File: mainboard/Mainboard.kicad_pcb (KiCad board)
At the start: 4 copper layers, 106 x 80 mm, 142 parts, among them IC1001 TXB0104RUT, IC1002 PCA9306JK, IC1003 TXB0104RUT, IC1101 PCAL6416AHF, IC1102 TMP117xxYBG, IC1103 PCA9306JK, IC1104 PCA9633DP1,118, IC1105 RV-8263-C8, IC1201 TXB0102DCU, IC1202 PCA9306JK, IC701 USBLC6-2P6, IC702 BQ21040DBV, IC703 MAX17048, IC801 TPS62823DLC, IC802 LP5907MFX-2.8, IC803 LP5907MFX-1.5, IC804 LP5907MFX-3.0, IC805 LP5907MFX-2.8, IC806 LP5907MFX-1.2, M901 ESP32-S3-WROOM-1, Q1101 DMN2053UQ, Q1102 DMN2053UQ, Q701 Si2333CDS, SW701 On / Off, SW901 Reset, X1001 LEPTON, X1201 Camera, X1301 Micro SD-Card, X1401 Displayboard, X701 USB, X702 Battery, X901 Prog, Y1001 25 MHz, Y1201 25 MHz

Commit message: Bug: Issue #11
- Add missing name for net for TP701

Closes: #11

Signed-off-by: Daniel Kampert <danielkampert@kampis-elektroecke.de>
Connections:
- net Net-(IC702-OUT) renamed /Project Architecture/Battery/VBat
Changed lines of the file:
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@@
 	(net 114 "/Project Architecture/Display/~{Display-Expander-Int}")
 	(net 115 "Net-(IC701-VBUS)")
-	(net 116 "Net-(IC702-OUT)")
+	(net 116 "/Project Architecture/Battery/VBat")
 	(net 117 "Net-(IC701-I{slash}O2-Pad3)")
 	(net 118 "Net-(IC701-I{slash}O1-Pad1)")
@@
 			(size 1 1)
 			(layers "F.Cu" "F.Mask")
-			(net 116 "Net-(IC702-OUT)")
+			(net 116 "/Project Architecture/Battery/VBat")
 			(pinfunction "1")
 			(pintype "passive")
@@
 			(layers "F.Cu" "F.Mask" "F.Paste")
 			(roundrect_rratio 0.25)
-			(net 116 "Net-(IC702-OUT)")
+			(net 116 "/Project Architecture/Battery/VBat")
 			(pinfunction "OUT")
 			(pintype "power_out")
@@
 			(layers "B.Cu" "B.Mask" "B.Paste")
 			(roundrect_rratio 0.25)
-			(net 116 "Net-(IC702-OUT)")
+			(net 116 "/Project Architecture/Battery/VBat")
 			(pintype "passive")
 		)
@@
 			(layers "B.Cu" "B.Mask" "B.Paste")
 			(roundrect_rratio 0.222222)
-			(net 116 "Net-(IC702-OUT)")
+			(net 116 "/Project Architecture/Battery/VBat")
 			(pintype "passive")
 		)
@@
 			(layers "B.Cu" "B.Mask" "B.Paste")
 			(roundrect_rratio 0.2)
-			(net 116 "Net-(IC702-OUT)")
+			(net 116 "/Project Architecture/Battery/VBat")
 			(pintype "passive")
 		)
@@
 			(layers "B.Cu" "B.Mask" "B.Paste")
 			(roundrect_rratio 0.222222)
-			(net 116 "Net-(IC702-OUT)")
+			(net 116 "/Project Architecture/Battery/VBat")
 			(pintype "passive")
 		)

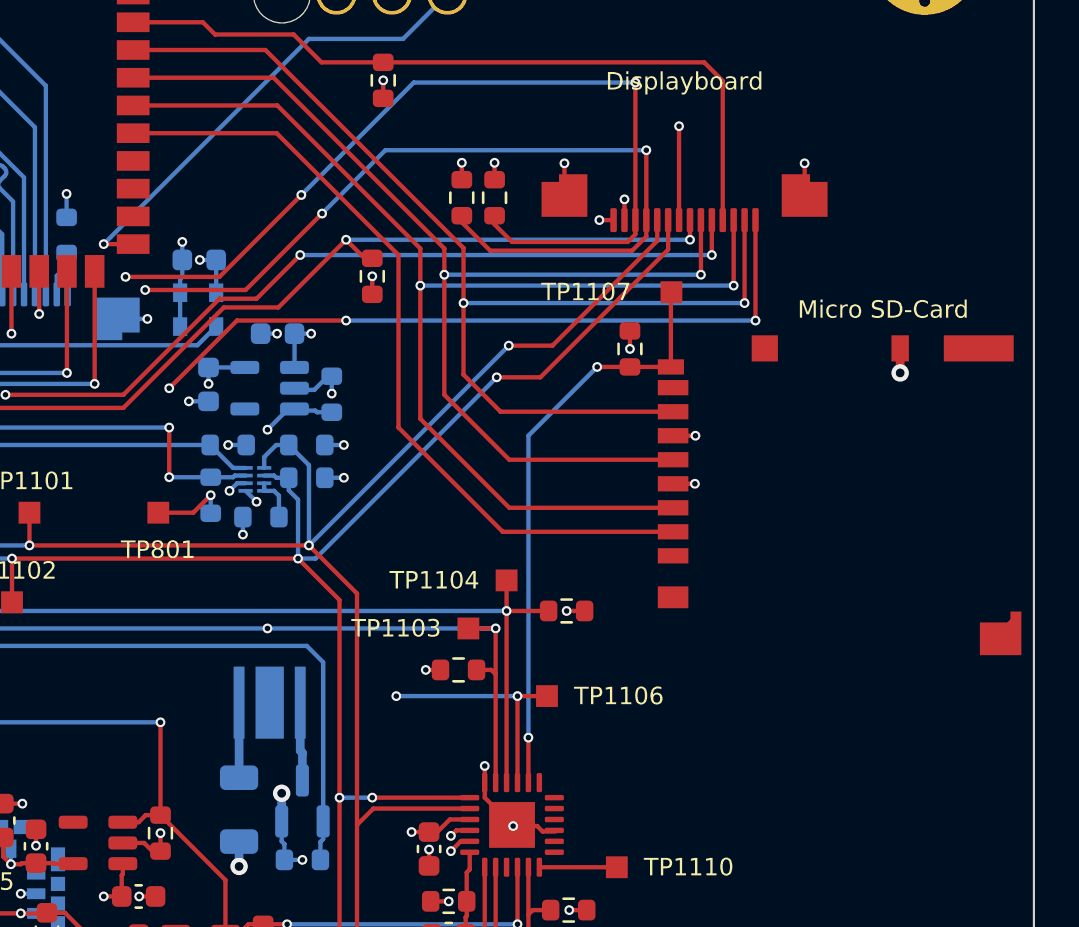
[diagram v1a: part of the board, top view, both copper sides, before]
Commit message: Feature: Issue #10
- Replace SD card holder with MSD-4-A

Closes: #10

Signed-off-by: Daniel Kampert <DanielKampert@kampis-elektroecke.de>
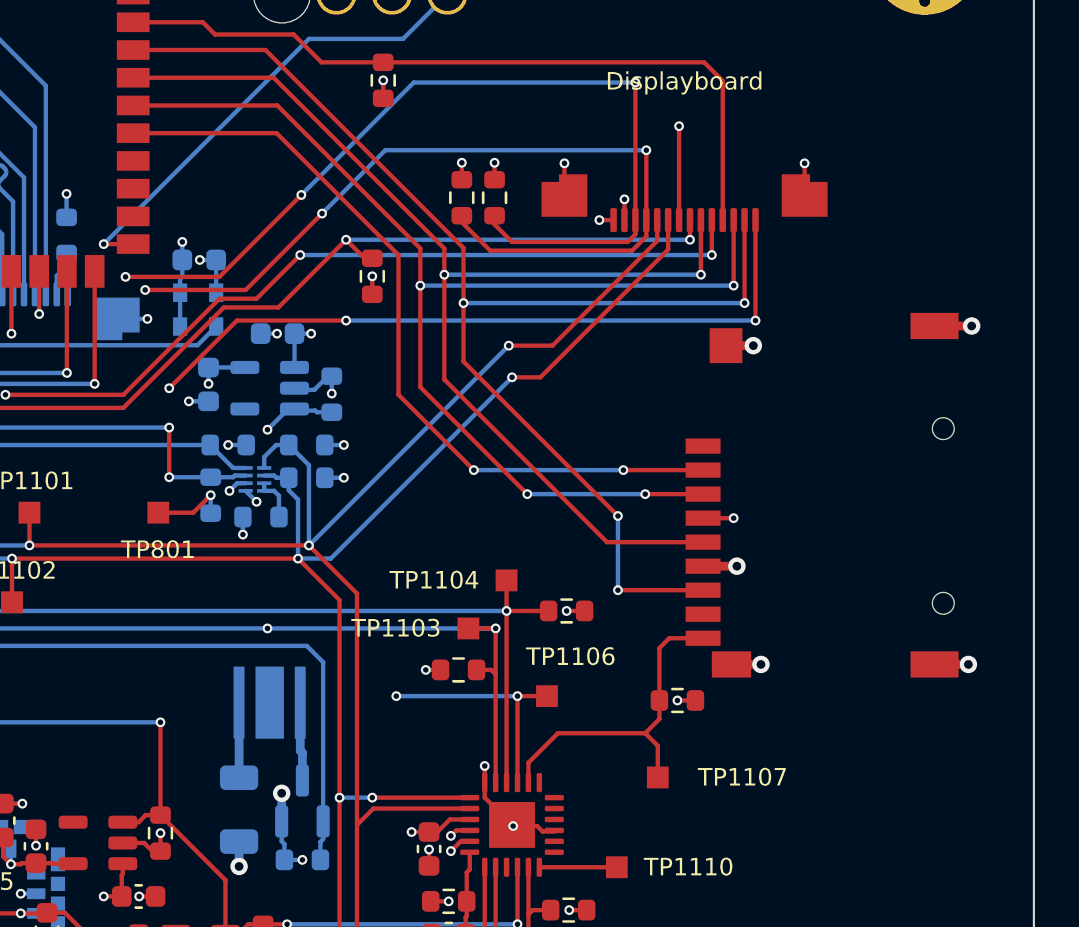
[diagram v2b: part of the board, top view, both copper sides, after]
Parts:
- X1301: footprint Connector_Card:microSD_HC_Hirose_DM3BT-DSF-PEJS -> Same Sky:MSD-4-A
- moved TP1107 22.2 mm to (248.8, 160.4), turned to 180 degrees
- moved R1301 16.2 mm to (249.7, 156.9), turned to 0 degrees
- moved X1301 1.50 mm to (258.6, 147.5)
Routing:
- net /Project Architecture/Peripherals/~{SD-CD}: track 27.2 -> 15.5 mm, vias 2 -> 0
- net /Project Architecture/Display/SPI-MISO: track 51.7 -> 58.1 mm, vias 2 -> 4
- net GND: track 123.0 -> 128.2 mm, vias 81 -> 84
- net /Project Architecture/Display/SPI-SCLK: track 50.1 -> 52.7 mm
- net /Project Architecture/MCU/~{SD-CS}: track 36.9 -> 36.2 mm, vias 0 -> 2
- net /Project Architecture/Display/SPI-MOSI: track 54.3 -> 54.5 mm, vias 2 -> 4

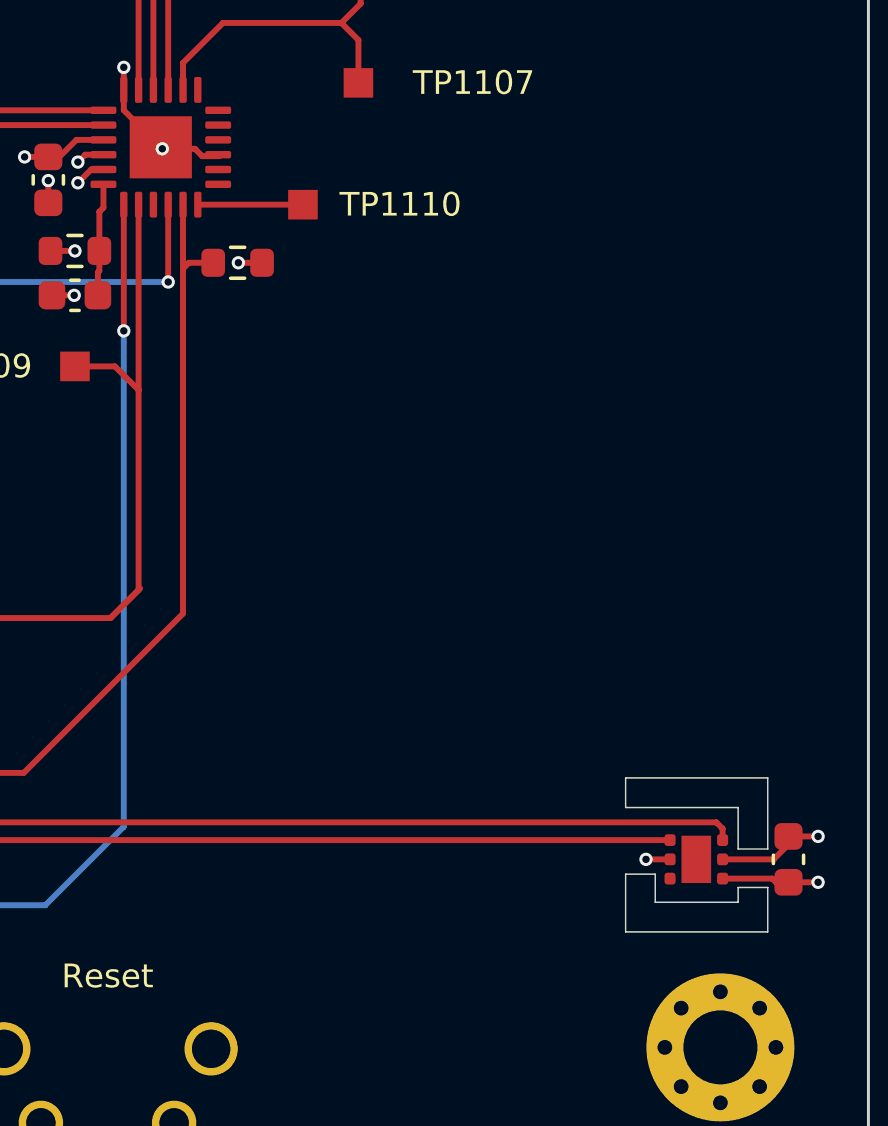
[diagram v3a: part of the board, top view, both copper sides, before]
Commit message: Feature: Issue #21
- Connect the TMP117 temperatur alert pin
- Add CI/CD workflow to check for changelog updates on pull requests

Closes #21

Signed-off-by: Daniel Kampert <DanielKampert@kampis-elektroecke.de>
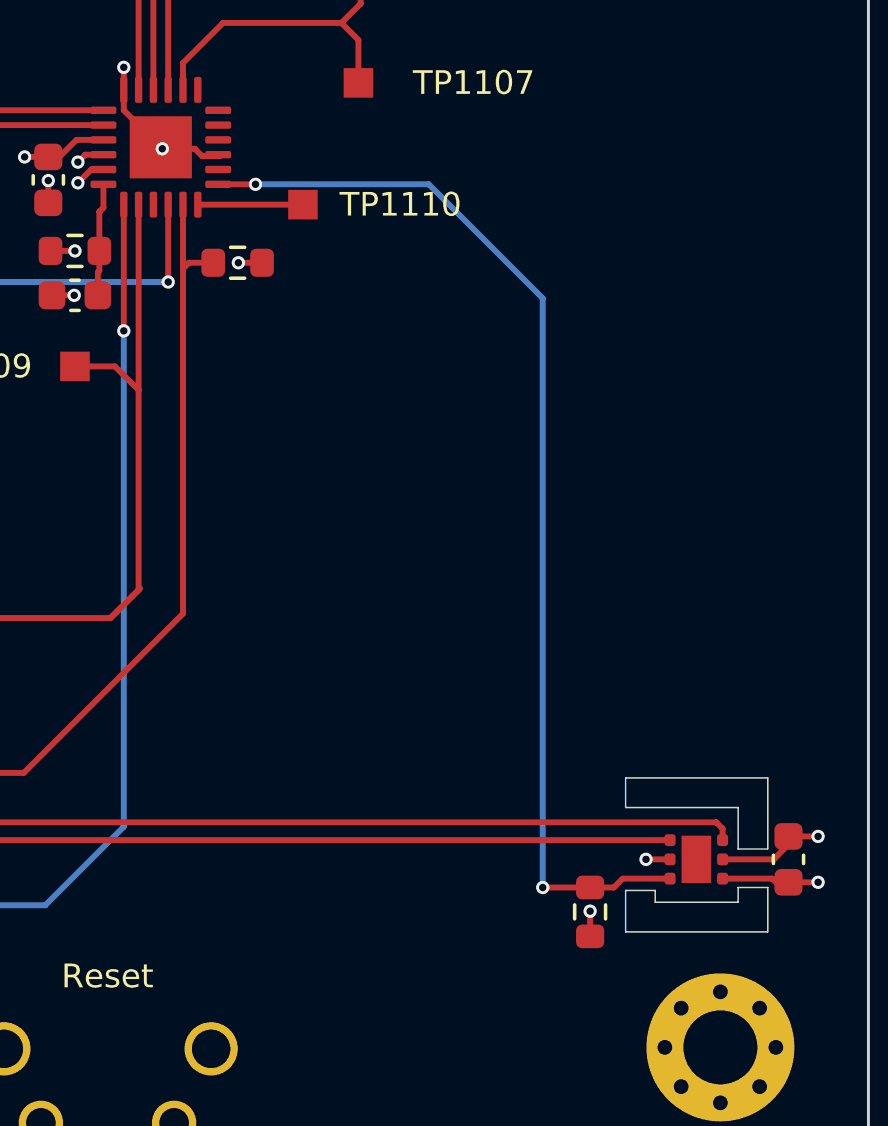
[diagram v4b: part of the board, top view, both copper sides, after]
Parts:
- added R1113: 3k3, Resistor_SMD:R_0603_1608Metric, F.Cu at (256.6, 188.4)
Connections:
- IC1101 pad 7: unconnected-(IC1101-P0_6-Pad7) -> /Project Architecture/Peripherals/~{TEMP-INT}
- IC1102 pad 3: unconnected-(IC1102-ALERT-Pad3) -> /Project Architecture/Peripherals/~{TEMP-INT}
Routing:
- net /Project Architecture/Peripherals/~{TEMP-INT}: track 0.00 -> 36.9 mm, vias 0 -> 2
- net +3V3: track 57.4 -> 58.3 mm, vias 39 -> 40
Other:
- outline, holes or cut-outs redrawn
